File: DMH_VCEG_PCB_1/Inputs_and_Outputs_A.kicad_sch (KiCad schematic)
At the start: 35 parts, among them J1 TS_Jack_6.35mm_Sw, J10 TS_Jack_6.35mm_Sw, J2 TS_Jack_6.35mm_Sw, J200 IDC_02x08, J21 Conn_01x10_PinHeader, J22 Conn_01x10_PinHeader, J23 Conn_01x10_PinHeader, J27 Conn_01x06_PinHeader, J3 TS_Jack_6.35mm_Sw, J4 TS_Jack_6.35mm_Sw, J5 TS_Jack_6.35mm_Sw, J6 TS_Jack_6.35mm_Sw, J7 TS_Jack_6.35mm_Sw, J8 TS_Jack_6.35mm_Sw, J9 TS_Jack_6.35mm_Sw, U21 TL072, U9 TL074

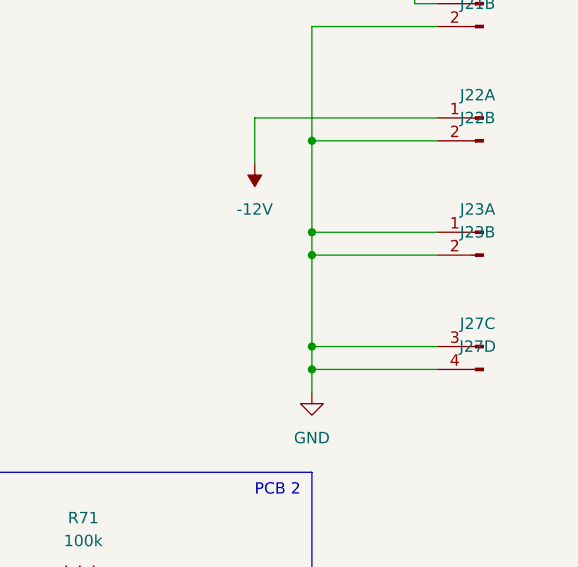
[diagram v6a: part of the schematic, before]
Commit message: Copied Manual Gate circuit to PCB 1 schematic
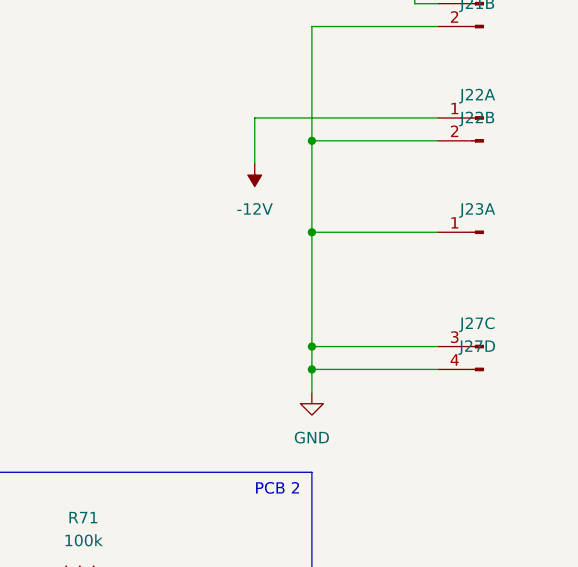
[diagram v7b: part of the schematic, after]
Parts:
- removed unit 2 of J23
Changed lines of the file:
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@@
-	)
-	(junction
-		(at 171.45 179.07)
-		(diameter 0)
-		(color 0 0 0 0)
 	)
 	(junction
@@
 	(wire
 		(pts
-			(xy 171.45 176.53) (xy 171.45 179.07)
-		)
-		(stroke
-			(width 0)
-			(type default)
-		)
-	)
-	(wire
-		(pts
 			(xy 171.45 176.53) (xy 185.42 176.53)
 		)
@@
 	(wire
 		(pts
-			(xy 185.42 179.07) (xy 171.45 179.07)
-		)
-		(stroke
-			(width 0)
-			(type default)
-		)
-	)
-	(wire
-		(pts
 			(xy 50.8 251.46) (xy 38.1 251.46)
 		)
@@
 	(wire
 		(pts
-			(xy 171.45 179.07) (xy 171.45 189.23)
+			(xy 171.45 176.53) (xy 171.45 189.23)
 		)
 		(stroke
@@
 				)
 			)
-		)
-	)
-	(symbol
-		(lib_id "SynthStuff:Conn_01x10_PinHeader")
-		(at 190.5 179.07 180)
-		(unit 2)
-		(exclude_from_sim no)
-		(in_bom yes)
-		(on_board yes)
-		(dnp no)
-		(fields_autoplaced yes)
-		(property "Reference" "J23"
-			(at 189.865 176.53 0)
-			(effects
-				(font
-					(size 1.27 1.27)
-				)
-			)
-		)
-		(property "Value" "Conn_01x10_PinHeader"
-			(at 190.5 176.53 0)
-			(effects
-				(font
-					(size 1.27 1.27)
-				)
-				(hide yes)
-			)
-		)
-		(property "Footprint" "Connector_PinHeader_2.54mm:PinHeader_1x10_P2.54mm_Vertical"
-			(at 190.5 179.07 0)
-			(effects
-				(font
-					(size 1.27 1.27)
-				)
-				(hide yes)
-			)
-		)
-		(property "Datasheet" "~"
-			(at 190.5 179.07 0)
-			(effects
-				(font
-					(size 1.27 1.27)
-				)
-				(hide yes)
-			)
-		)
-		(property "Description" "Generic connector, single row, 01x10"
-			(at 190.5 179.07 0)
-			(effects
-				(font
-					(size 1.27 1.27)
-				)
-				(hide yes)
-			)
-		)
-		(pin "5"
-		)
-		(pin "10"
-		)
-		(pin "2"
-		)
-		(pin "9"
-		)
-		(pin "3"
-		)
-		(pin "8"
-		)
-		(pin "1"
-		)
-		(pin "4"
-		)
-		(pin "6"
-		)
-		(pin "7"
-		)
-		(instances
-			(project "DMH_VCEG_PCB_1"
-				(path "/58f4306d-5387-4983-bb08-41a2313fd315/ce3fef8b-9f1d-4178-b50b-4a046c030679"
-					(reference "J23")
-					(unit 2)
-				)
-			)

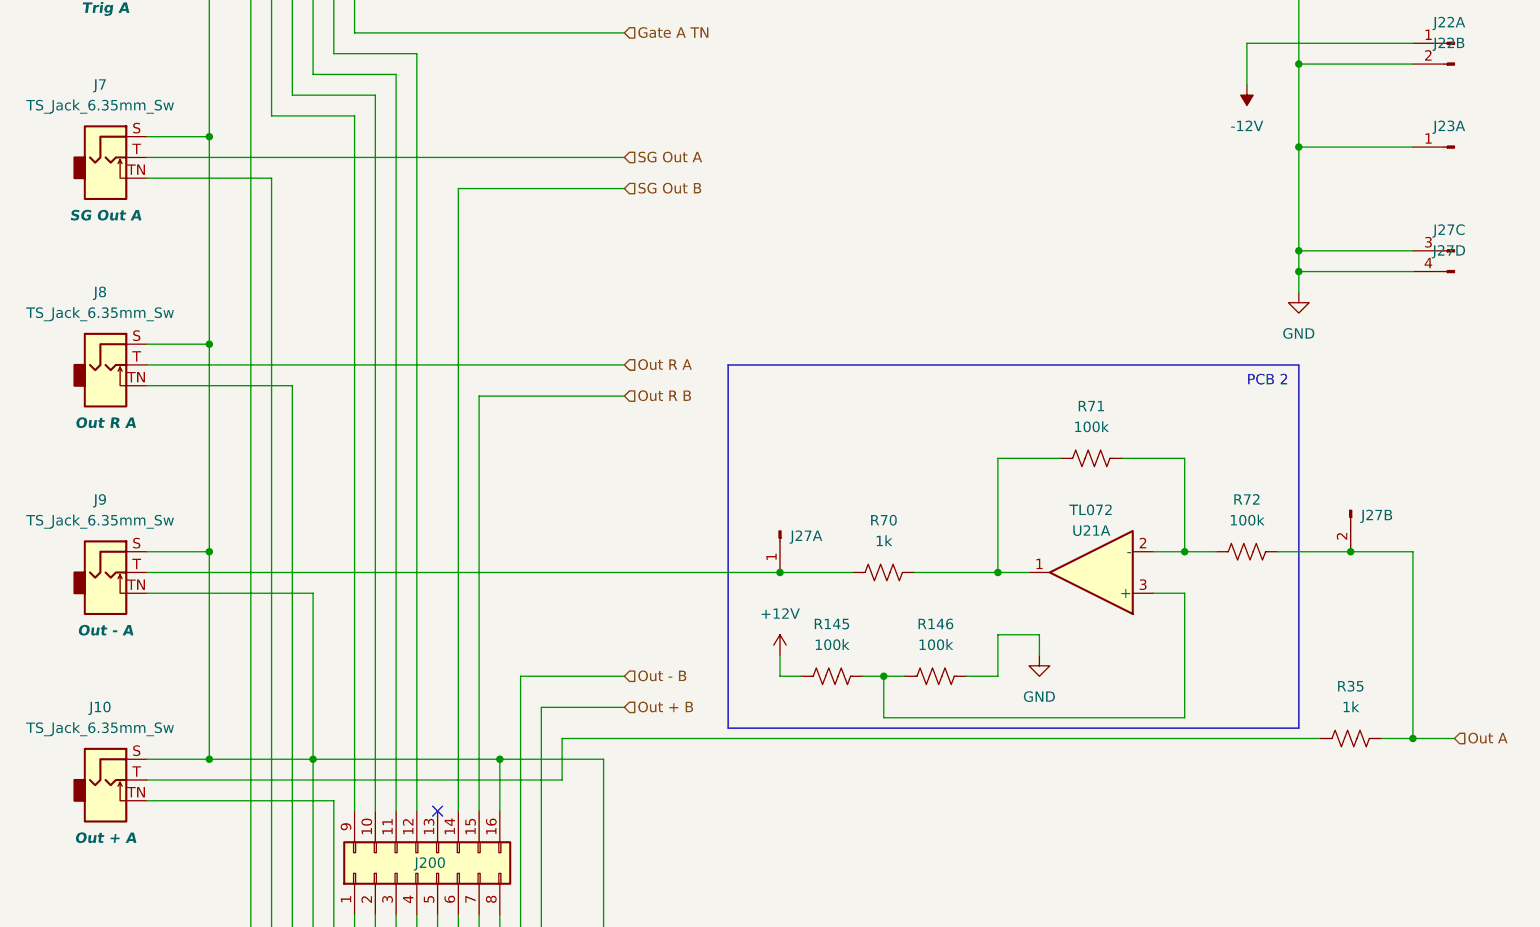
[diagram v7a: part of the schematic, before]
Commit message: Added Output attenuation circuit
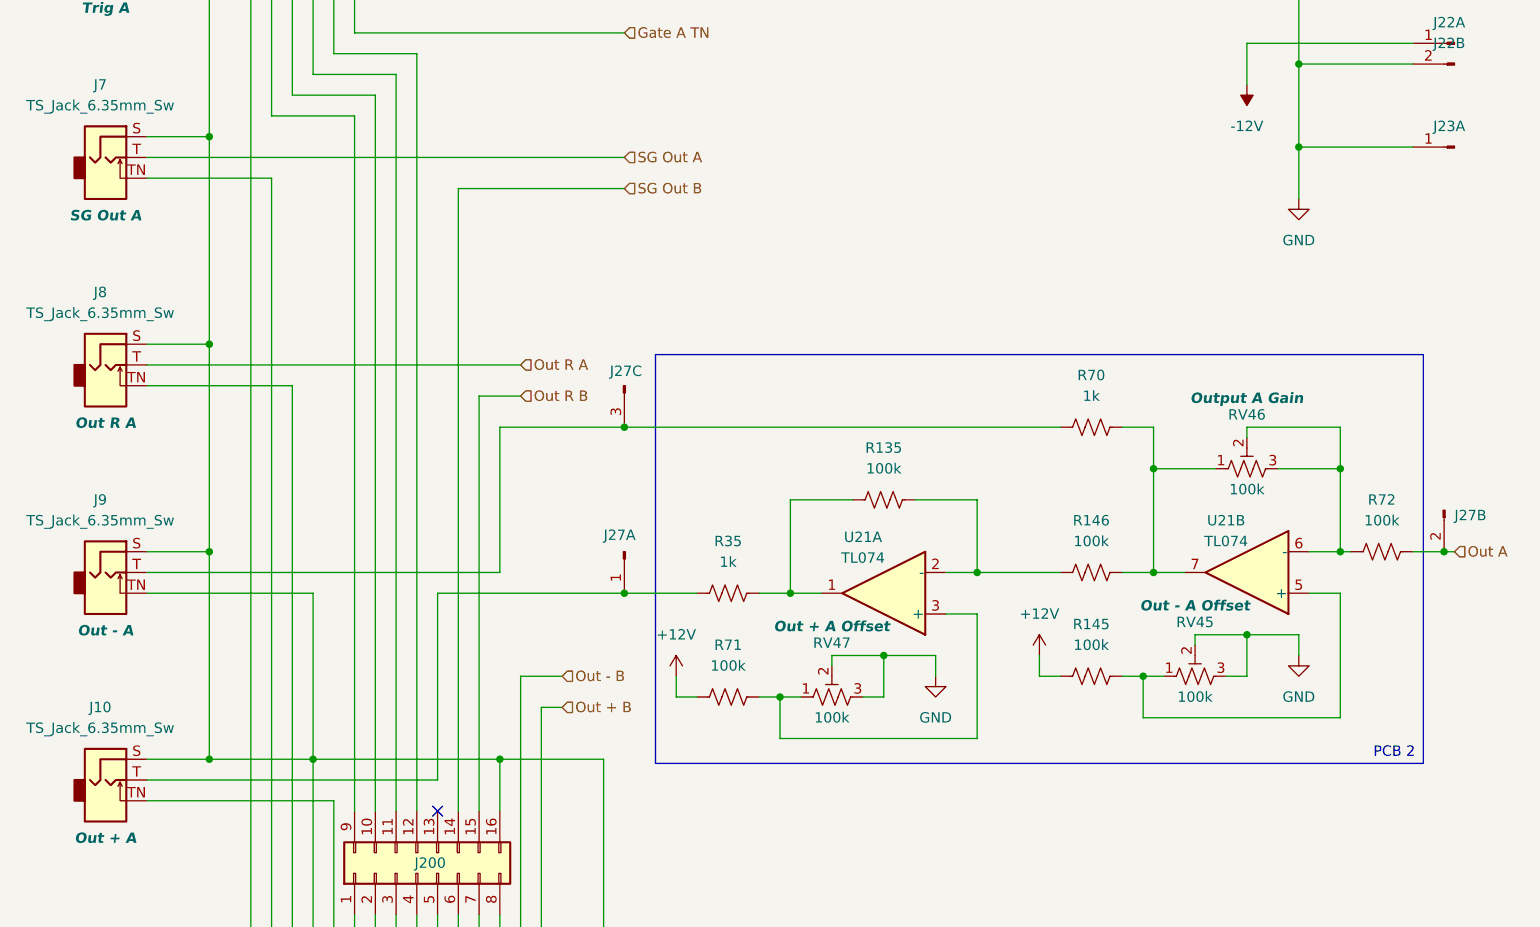
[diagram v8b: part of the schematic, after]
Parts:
- removed unit 4 of J27
- removed U21: TL072, Package_DIP:DIP-8_W7.62mm_Socket, symbol Amplifier_Operational:TL072
- added R135: 100k, Resistor_THT:R_Axial_DIN0207_L6.3mm_D2.5mm_P7.62mm_Horizontal, symbol Device:R_US
- added RV45, RV46, RV47: 100k, Potentiometer_THT:Potentiometer_Bourns_3296X_Horizontal, symbol Device:R_Potentiometer_Trim_US
- added U21: TL074, Package_DIP:DIP-14_W7.62mm_Socket, symbol Amplifier_Operational:TL074
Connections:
- net +12V: now also R71.2
- net GND: now also RV45.2, RV45.3, RV47.2, RV47.3; no longer J27.3 (Pin_3), R146.1
- net Out A: no longer R35.1
- net at R72.2: now also RV46.2, RV46.3, U21.6 (-); no longer R71.1
- net at J9.T, R70.2: now also J27.3 (Pin_3); no longer J27.1 (Pin_1)
- net at J10.T, R35.2: now also J27.1 (Pin_1)
- net at R70.1: now also R146.1, RV46.1, U21.7; no longer R71.2
- net at R145.1: now also RV45.1, U21.5 (+); no longer R146.2
- new net: R71.1, RV47.1, U21.3 (+)
- new net: R135.2, R35.1, U21.1
- new net: R135.1, R146.2, U21.2 (-)
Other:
- moved on the sheet: J27B, R145, R35, R70, R72
